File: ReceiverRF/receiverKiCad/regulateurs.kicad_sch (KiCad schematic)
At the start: 7 parts, among them J1 Conn_01x02, U2 AP2210N-3.3TRG1, U3 LP2980AIM5-5.0/NOPB

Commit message: finir layout schematic et création projet firmware pour rfreceiver
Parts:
- added D? (x2): Rouge, footprint-receiver:LTST-C190EKT, symbol Device:LED
- added R?: 145, symbol Device:R
- added R?: 315, symbol Device:R
- renumbered U2 to U4
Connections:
- net GND: now also C4.2, D?.1 (K), D?.1 (K)
- net VIN: now reaches C1.1, C3.1, J1.1 (Pin_1), U3.1 (Vin), U3.3 (ON), U4.3 (VIN)
- net 3.3V renamed +3.3V
- net +3.3V: now also R?.1
- net 5V renamed +5V
- net +5V: now also R?.1
- new net: D?.2 (A), R?.2 (x2)
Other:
- note added: "Connecteur batterie Vin (max 15V)"
- note added: "Limite courant à 10mA Vf 1.85V pour diode rouge"
- note added: "Régulateur 3.3V"
- note added: "Régulateur 5V"
- moved on the sheet: C1, C2, C3, C4, J1, U3, U4

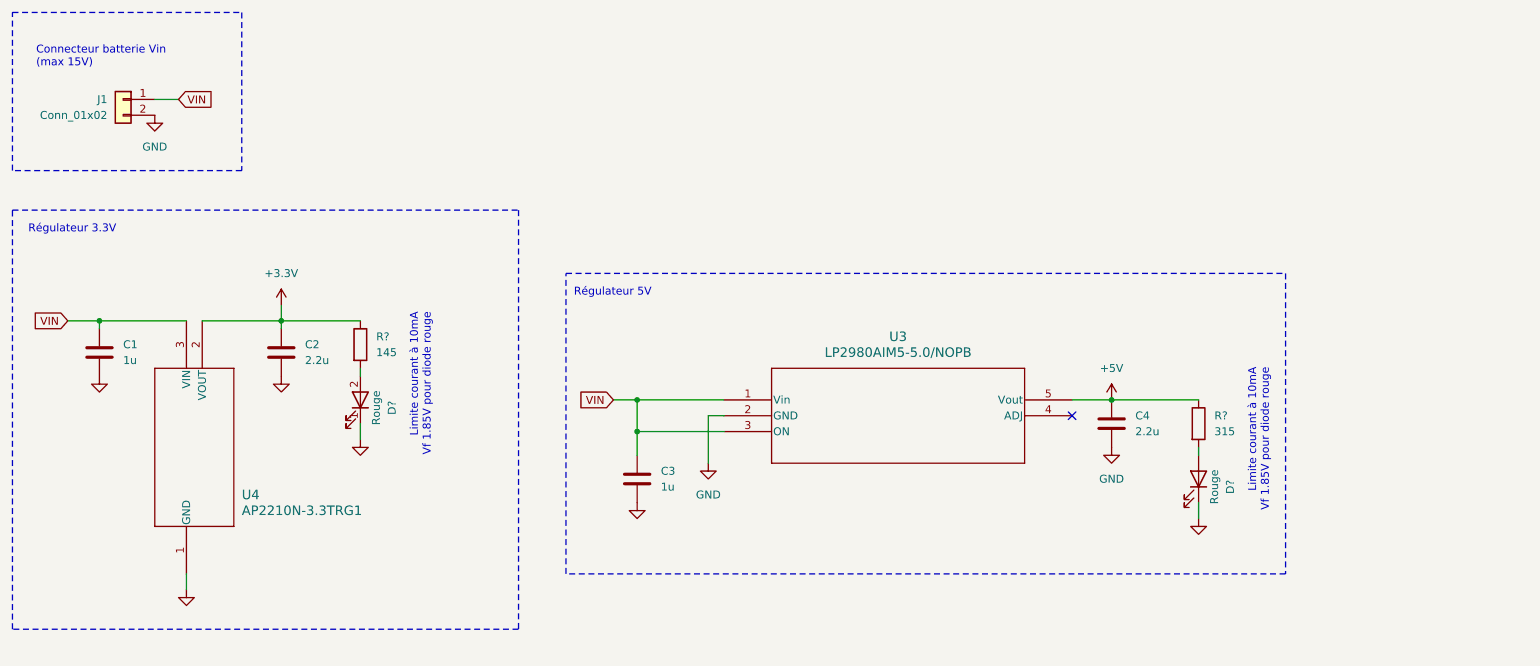
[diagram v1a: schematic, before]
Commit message: Changement régulateurs, meilleur circuit debouncing boutons, documentation
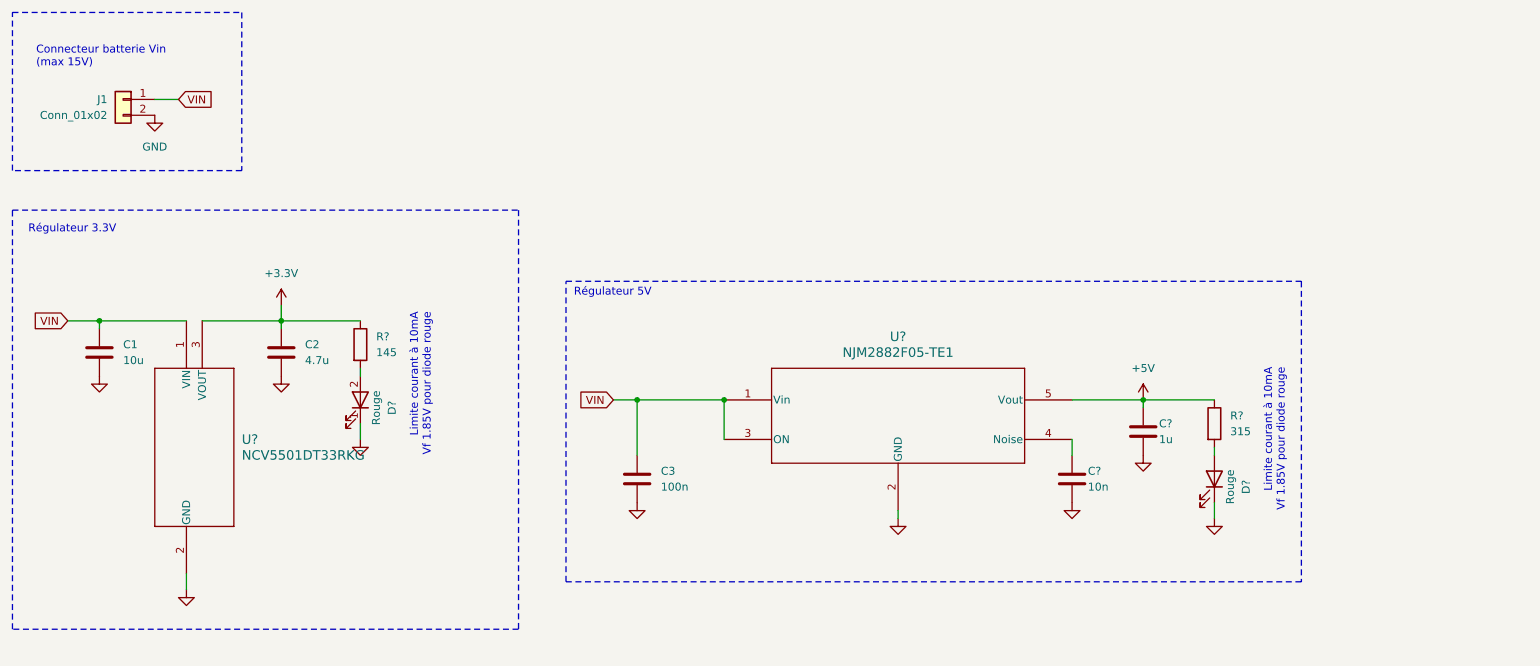
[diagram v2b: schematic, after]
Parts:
- removed U3: LP2980AIM5-5.0/NOPB, MF05A_TEX, symbol symbol-receiver:LP2980AIM5-5.0_NOPB
- removed U4: AP2210N-3.3TRG1, SOT_3.3TRG1_DIO, symbol symbol-receiver:AP2210N-3.3TRG1
- added C?: 10n, symbol Device:C
- added U?: NJM2882F05-TE1, footprint-receiver:SOT-23-5, symbol symbol-receiver:NJM2882F05-TE1
- added U?: NCV5501DT33RKG, footprint-receiver:DPAK-3_ONS-M, symbol symbol-receiver:NCV5501DT33RKG
- C1: value 1u -> 10u
- C2: value 2.2u -> 4.7u
- C3: value 1u -> 100n
- C?: renamed from C4; value 2.2u -> 1u
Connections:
- net +3.3V: now also U?.3 (VOUT)
- net +5V: now also U?.5 (Vout)
- net GND: now also C?.2, U?.2 (GND), U?.2 (GND)
- net VIN: now also U?.1 (VIN), U?.1 (Vin), U?.3 (ON)
- new net: C?.1, U?.4 (Noise)
- no-connect marks 1 -> 0
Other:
- moved on the sheet: C?, D?, R?

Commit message: Corrige path footprints
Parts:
- D? (x2): footprint footprint-receiver:LTST-C190EKT -> Footprints:LTST-C190EKT
- U?: footprint footprint-receiver:SOT-23-5 -> Footprints:SOT-23-5
- U?: footprint footprint-receiver:DPAK-3_ONS-M -> Footprints:DPAK-3_ONS-M
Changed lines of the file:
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@@
 			)
 		)
-		(property "Footprint" "footprint-receiver:SOT-23-5"
+		(property "Footprint" "Footprints:SOT-23-5"
 			(at 134.62 77.47 0)
 			(effects
@@
 			)
 		)
-		(property "Footprint" "footprint-receiver:LTST-C190EKT"
+		(property "Footprint" "Footprints:LTST-C190EKT"
 			(at 76.2 81.28 0)
 			(effects
@@
 			)
 		)
-		(property "Footprint" "footprint-receiver:DPAK-3_ONS-M"
+		(property "Footprint" "Footprints:DPAK-3_ONS-M"
 			(at 44.45 109.22 0)
 			(effects
@@
 			)
 		)
-		(property "Footprint" "footprint-receiver:LTST-C190EKT"
+		(property "Footprint" "Footprints:LTST-C190EKT"
 			(at 213.36 93.98 0)
 			(effects

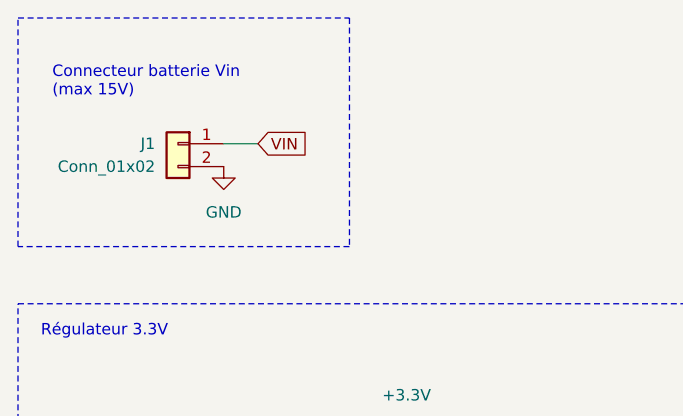
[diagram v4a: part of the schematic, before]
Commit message: Ajout footprint et circuit pour potentiomètre volume, push button, on/off switch
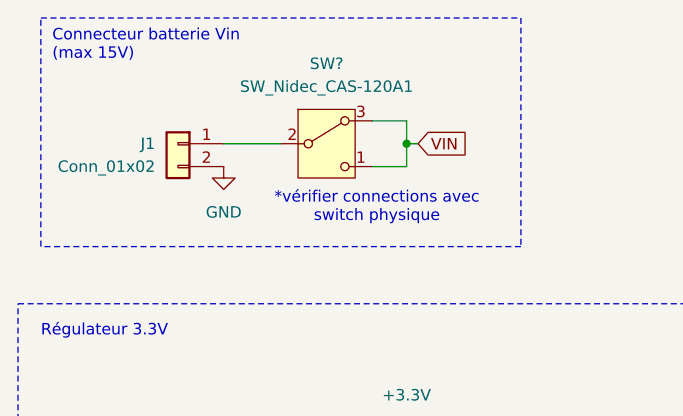
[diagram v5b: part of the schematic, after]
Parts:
- added SW?: SW_Nidec_CAS-120A1, Footprints:Toggle_SW, symbol Switch:SW_Nidec_CAS-120A1
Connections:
- net VIN: now also SW?.1 (C), SW?.3 (A); no longer J1.1 (Pin_1)
- new net: J1.1 (Pin_1), SW?.2 (B)
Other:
- note added: "*vérifier connections avec switch physique"
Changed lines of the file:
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@@
 		(color 0 0 0 0)
 	)
+	(junction
+		(at 63.5 33.02)
+		(diameter 0)
+		(color 0 0 0 0)
+	)
 	(wire
 		(pts
@@
 	(wire
 		(pts
+			(xy 63.5 30.48) (xy 59.69 30.48)
+		)
+		(stroke
+			(width 0)
+			(type default)
+		)
+	)
+	(wire
+		(pts
 			(xy 50.8 68.58) (xy 63.5 68.58)
 		)
@@
 	(wire
 		(pts
+			(xy 63.5 35.56) (xy 63.5 33.02)
+		)
+		(stroke
+			(width 0)
+			(type default)
+		)
+	)
+	(wire
+		(pts
+			(xy 63.5 33.02) (xy 63.5 30.48)
+		)
+		(stroke
+			(width 0)
+			(type default)
+		)
+	)
+	(wire
+		(pts
+			(xy 59.69 35.56) (xy 63.5 35.56)
+		)
+		(stroke
+			(width 0)
+			(type default)
+		)
+	)
+	(wire
+		(pts
+			(xy 63.5 33.02) (xy 64.77 33.02)
+		)
+		(stroke
+			(width 0)
+			(type default)
+		)
+	)
+	(wire
+		(pts
 			(xy 76.2 85.09) (xy 76.2 87.63)
 		)
@@
 	(wire
 		(pts
-			(xy 43.18 33.02) (xy 46.99 33.02)
-		)
-		(stroke
-			(width 0)
-			(type default)
-		)
-	)
-	(wire
-		(pts
 			(xy 63.5 68.58) (xy 63.5 69.85)
 		)
@@
 		(pts
 			(xy 190.5 87.63) (xy 190.5 90.17)
+		)
+		(stroke
+			(width 0)
+			(type default)
+		)
+	)
+	(wire
+		(pts
+			(xy 43.18 33.02) (xy 49.53 33.02)
 		)
 		(stroke
@@
 	)
 	(rectangle
-		(start 20.32 19.05)
-		(end 57.15 44.45)
+		(start 22.86 19.05)
+		(end 76.2 44.45)
 		(stroke
 			(width 0)
@@
 	(text "Connecteur batterie Vin\n(max 15V)"
 		(exclude_from_sim no)
-		(at 24.13 27.94 0)
+		(at 24.13 23.876 0)
 		(effects
 			(font
@@
 			)
 			(justify left bottom)
+		)
+	)
+	(text "*vérifier connections avec\nswitch physique"
+		(exclude_from_sim no)
+		(at 60.198 40.132 0)
+		(effects
+			(font
+				(size 1.27 1.27)
+			)
 		)
 	)
@@
 	(global_label "VIN"
 		(shape input)
-		(at 46.99 33.02 0)
+		(at 64.77 33.02 0)
 		(fields_autoplaced yes)
 		(effects
@@
 		)
 		(property "Intersheetrefs" "${INTERSHEET_REFS}"
-			(at 52.9991 33.02 0)
+			(at 70.7791 33.02 0)
 			(effects
 				(font
@@
 					(unit 1)
 				)
+			)
+		)
+	)
+	(symbol
+		(lib_id "Switch:SW_Nidec_CAS-120A1")
+		(at 54.61 33.02 0)
+		(unit 1)
+		(exclude_from_sim no)
+		(in_bom yes)
+		(on_board yes)
+		(dnp no)
+		(fields_autoplaced yes)
+		(property "Reference" "SW?"
+			(at 54.61 24.13 0)
+			(effects
+				(font
+					(size 1.27 1.27)
+				)
+			)
+		)
+		(property "Value" "SW_Nidec_CAS-120A1"
+			(at 54.61 26.67 0)
+			(effects
+				(font
+					(size 1.27 1.27)
+				)
+			)
+		)
+		(property "Footprint" "Footprints:Toggle_SW"
+			(at 54.61 43.18 0)
+			(effects
+				(font
+					(size 1.27 1.27)
+				)
+				(hide yes)
+			)
+		)
+		(property "Datasheet" "https://www.digikey.com/en/products/detail/c-k/7301SYZQE/7080"
+			(at 54.61 40.64 0)
+			(effects
+				(font
+					(size 1.27 1.27)
+				)
+				(hide yes)
+			)
+		)
+		(property "Description" "Switch, single pole double throw"
+			(at 54.61 33.02 0)
+			(effects
+				(font
+					(size 1.27 1.27)
+				)
+				(hide yes)
+			)
+		)
+		(pin "3"
+		)
+		(pin "2"
+		)
+		(pin "1"
+		)
+		(instances
+			(project ""
+				(path "/439ba515-58d4-4b14-87ab-b438dcf423a5/daa1b3d3-1e11-4b02-868f-dd095818f20a"
+					(reference "SW?")
+					(unit 1)
+				)

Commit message: Identifiants des symboles
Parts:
- gave numbers to parts that had none: 9
- renumbered C1 to PWR_C1, C2 to PWR_C2, C3 to PWR_C4, J1 to PWR_J1
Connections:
- net VIN renamed VCC
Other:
- note added: "POWER FLAGS"
- moved on the sheet: PWR_C5

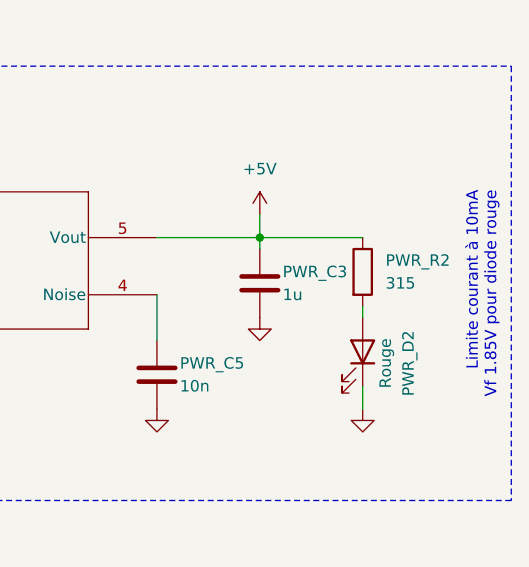
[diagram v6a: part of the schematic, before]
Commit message: Footprint et choix composantes mineures (résistances et condo)
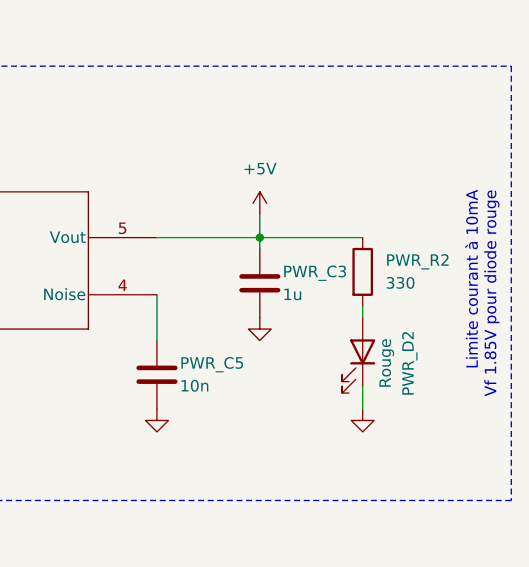
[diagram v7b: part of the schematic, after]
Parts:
- PWR_C1: footprint (none) -> Capacitor_SMD:C_1206_3216Metric
- PWR_C2, PWR_C3: footprint (none) -> Capacitor_SMD:C_0603_1608Metric
- PWR_C4, PWR_C5: footprint (none) -> Capacitor_SMD:C_0402_1005Metric
- PWR_R1: footprint (none) -> Resistor_SMD:R_1206_3216Metric
- PWR_R2: value 315 -> 330; footprint (none) -> Resistor_SMD:R_1206_3216Metric
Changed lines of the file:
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@@
 			)
 		)
-		(property "Footprint" ""
+		(property "Footprint" "Resistor_SMD:R_1206_3216Metric"
 			(at 74.422 72.39 90)
 			(effects
@@
 			)
 		)
-		(property "Footprint" ""
+		(property "Footprint" "Capacitor_SMD:C_0603_1608Metric"
 			(at 202.8952 90.17 0)
 			(effects
@@
 			)
 		)
-		(property "Footprint" ""
+		(property "Footprint" "Capacitor_SMD:C_0603_1608Metric"
 			(at 64.4652 77.47 0)
 			(effects
@@
 			)
 		)
-		(property "Footprint" ""
+		(property "Footprint" "Capacitor_SMD:C_0402_1005Metric"
 			(at 191.4652 100.33 0)
 			(effects
@@
 			)
 		)
-		(property "Footprint" ""
+		(property "Footprint" "Capacitor_SMD:C_0402_1005Metric"
 			(at 121.6152 97.79 0)
 			(effects
@@
 			)
 		)
-		(property "Footprint" ""
+		(property "Footprint" "Capacitor_SMD:C_1206_3216Metric"
 			(at 35.2552 77.47 0)
 			(effects
@@
 			)
 		)
-		(property "Value" "315"
+		(property "Value" "330"
 			(at 215.9 86.36 0)
 			(effects
@@
 			)
 		)
-		(property "Footprint" ""
+		(property "Footprint" "Resistor_SMD:R_1206_3216Metric"
 			(at 211.582 85.09 90)
 			(effects

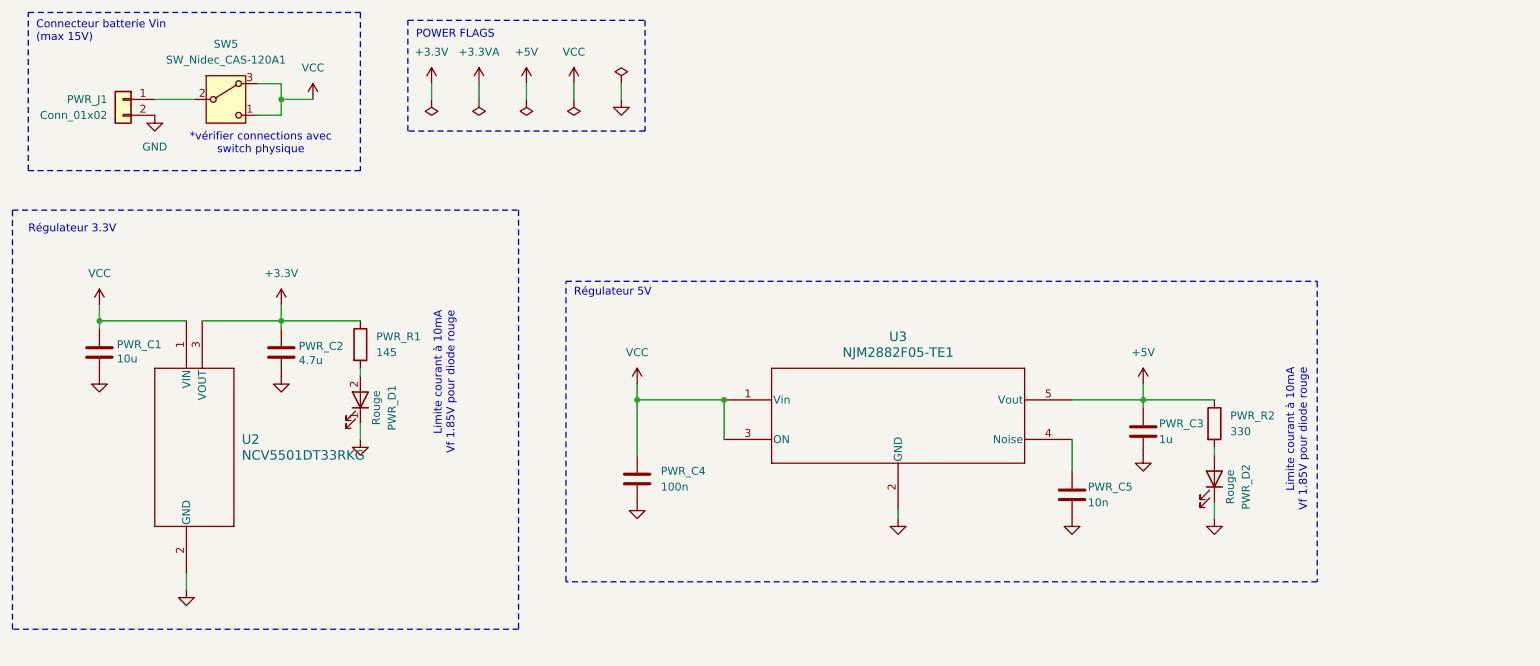
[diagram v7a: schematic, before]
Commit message: suggestions de Luca et placement sur PCB
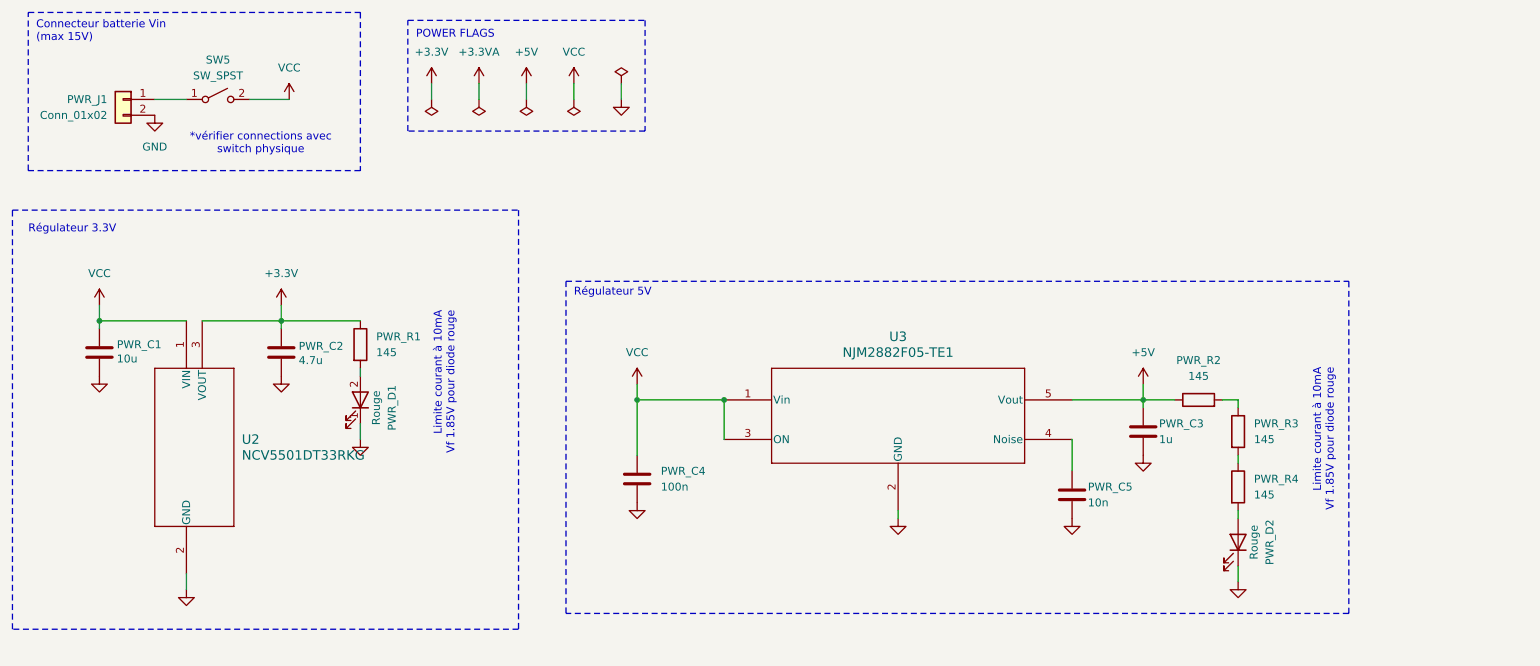
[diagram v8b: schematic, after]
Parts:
- removed SW5: SW_Nidec_CAS-120A1, Footprints:Toggle_SW, symbol Switch:SW_Nidec_CAS-120A1
- added PWR_R3, PWR_R4: 145, Resistor_SMD:R_1206_3216Metric, symbol Device:R
- added SW5: SW_SPST, Footprints:D102J12S215PQA_CNK, symbol Switch:SW_SPST
- PWR_R2: value 330 -> 145
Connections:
- net VCC: now also SW5.2 (B)
- net at PWR_J1.1 (Pin_1): now also SW5.1 (A)
- net at PWR_D2.2 (A): now also PWR_R4.2; no longer PWR_R2.2
- new net: PWR_R3.2, PWR_R4.1
- new net: PWR_R2.2, PWR_R3.1
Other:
- moved on the sheet: PWR_D2
